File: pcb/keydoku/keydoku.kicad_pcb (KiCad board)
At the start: 2 copper layers, 111 x 99.9 mm, 37 parts

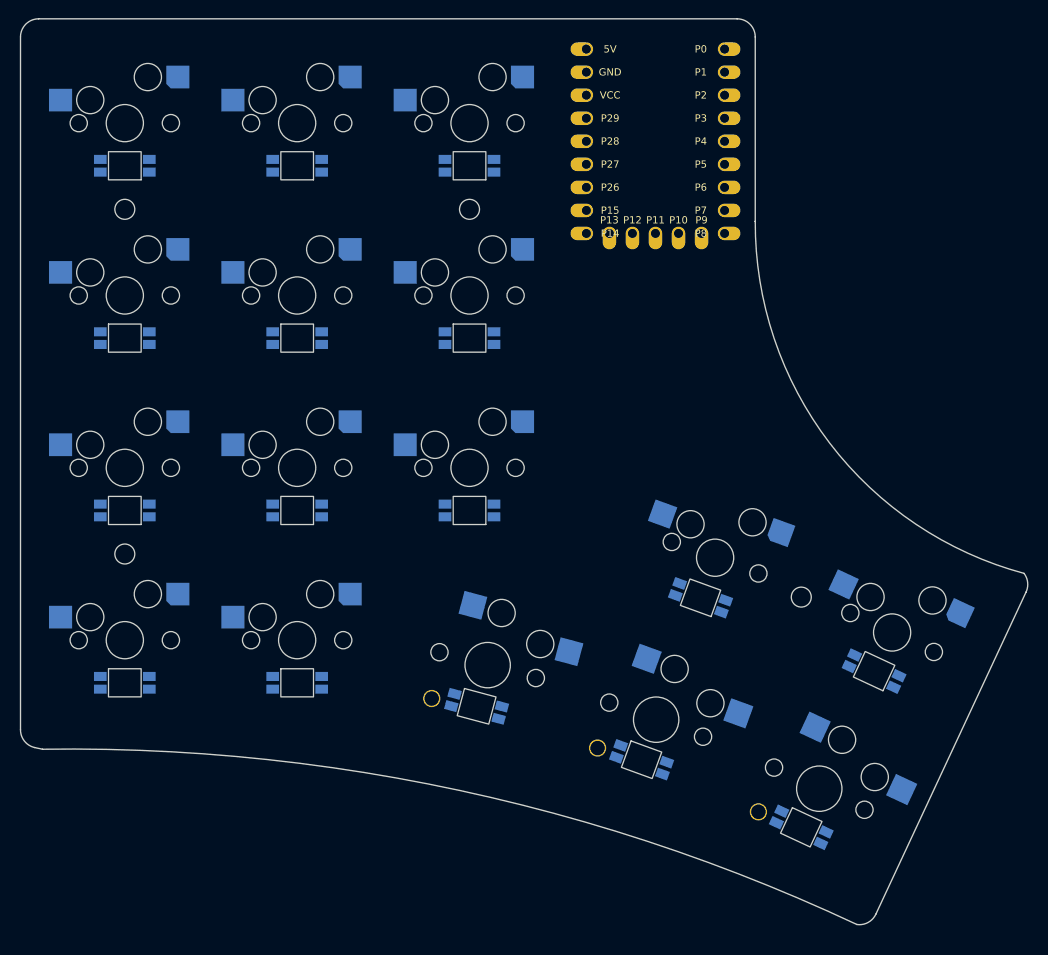
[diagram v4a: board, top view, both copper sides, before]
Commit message: Adding CTC logo as a footprint
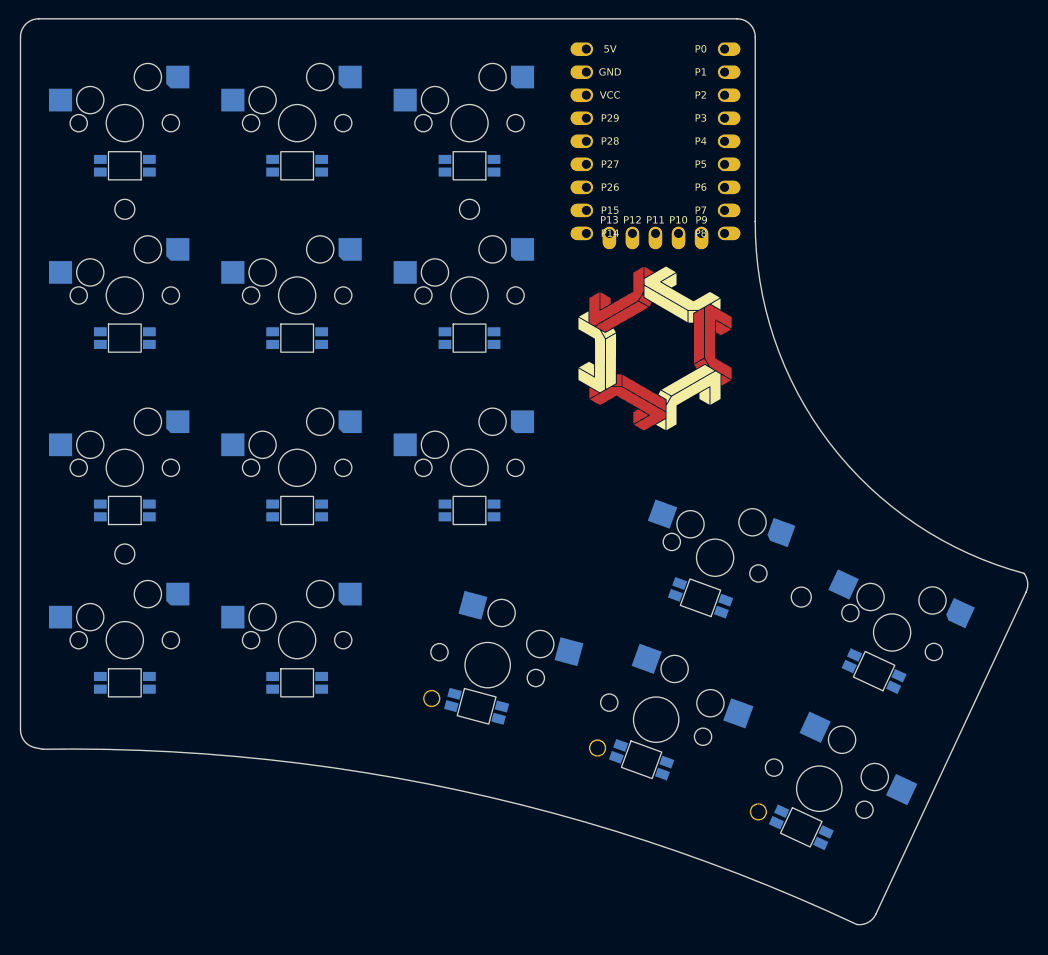
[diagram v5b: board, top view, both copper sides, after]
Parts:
- added G***: LOGO, Project:ctc, F.Cu at (158.4, 117.8)

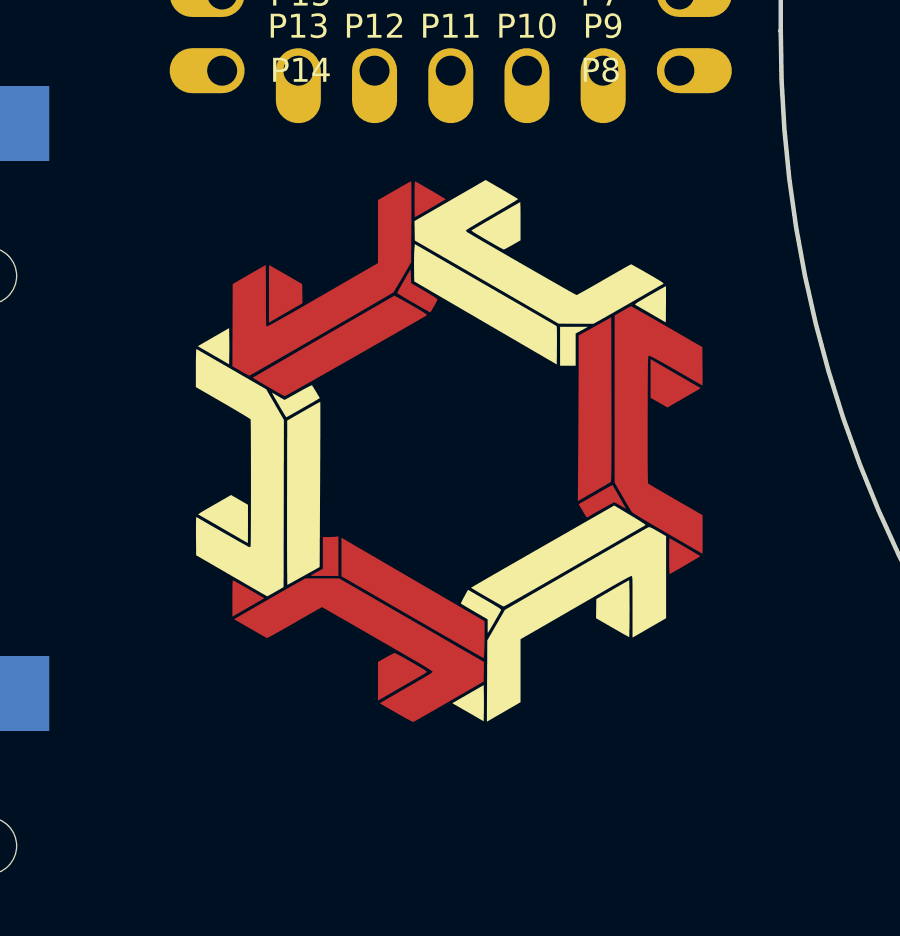
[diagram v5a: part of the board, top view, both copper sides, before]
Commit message: Rotate per key leds and add CTC footprint
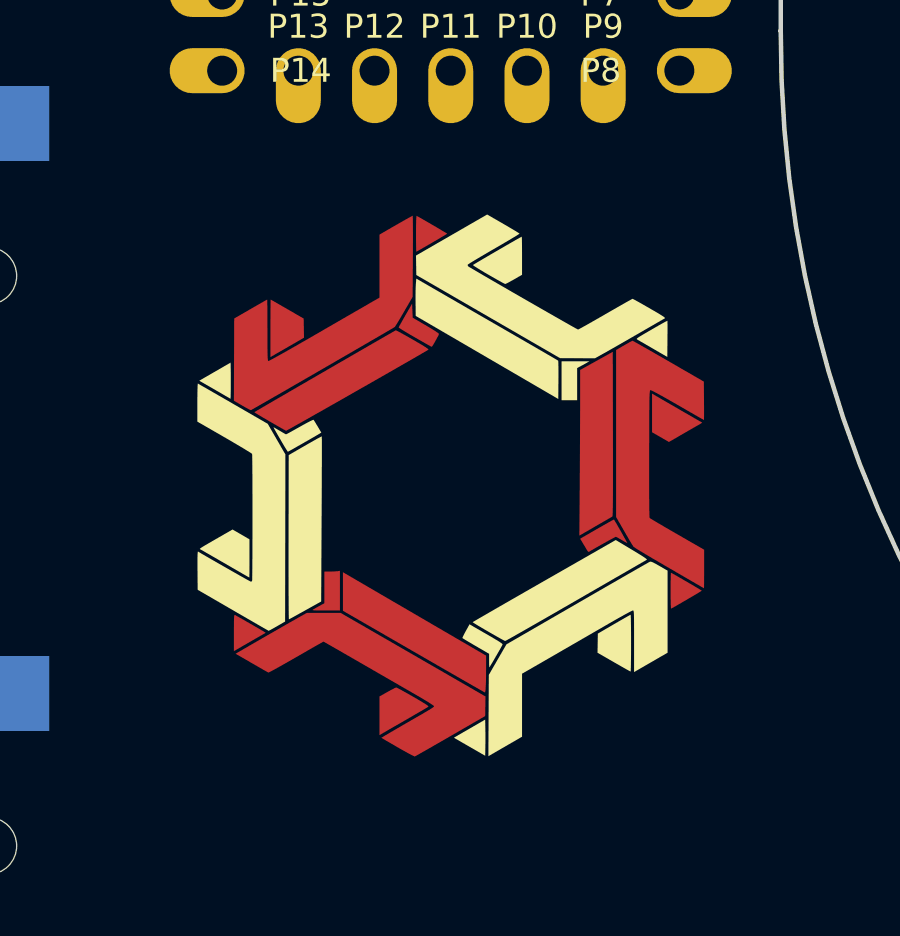
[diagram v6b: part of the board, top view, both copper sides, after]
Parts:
- moved G*** 1.15 mm to (158.5, 119.0)

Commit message: VCC traces in place
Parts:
- moved LED16 1.23 mm to (174.7, 171.9)
- moved LED5 1.23 mm to (138.1, 136.9)
- moved MH1 1.23 mm to (100.1, 103.7)
- moved LED15 1.23 mm to (157.1, 164.4)
- moved MH3 1.23 mm to (100.1, 141.7)
- moved S14 1.23 mm to (140.1, 154.0)
- moved LED6 1.23 mm to (138.1, 98.9)
- moved LED13 1.23 mm to (138.1, 117.9)
- moved LED1 1.23 mm to (100.1, 136.9)
- moved LED4 1.23 mm to (119.1, 98.9)
- moved MH4 1.23 mm to (174.7, 146.5)
- moved LED14 1.23 mm to (138.9, 158.5)
- moved S1 1.23 mm to (100.1, 151.2)
- moved S5 1.23 mm to (119.1, 151.2)
- moved MCU1 1.23 mm to (158.6, 96.2)
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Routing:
- net VCC5V: track 0.00 -> 375.3 mm, vias 0 -> 6

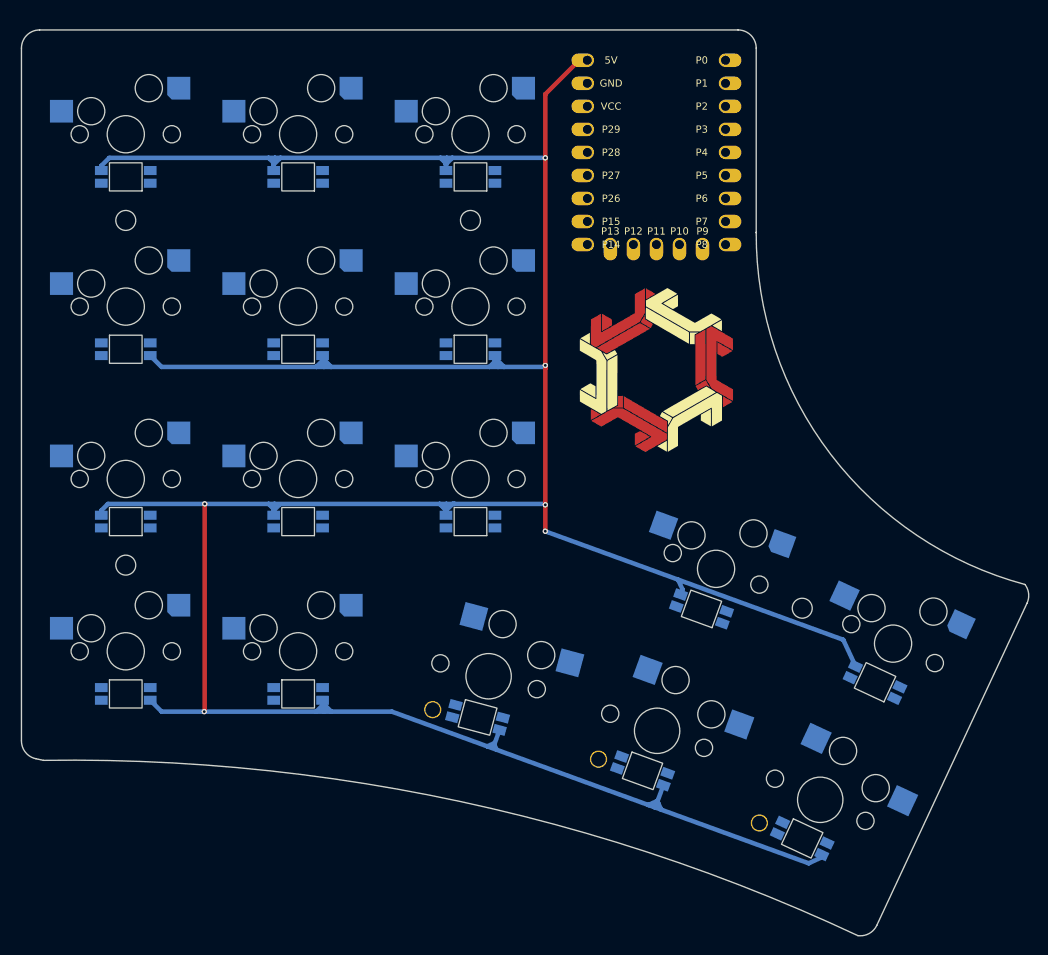
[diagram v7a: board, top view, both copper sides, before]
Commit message: All traces except GND
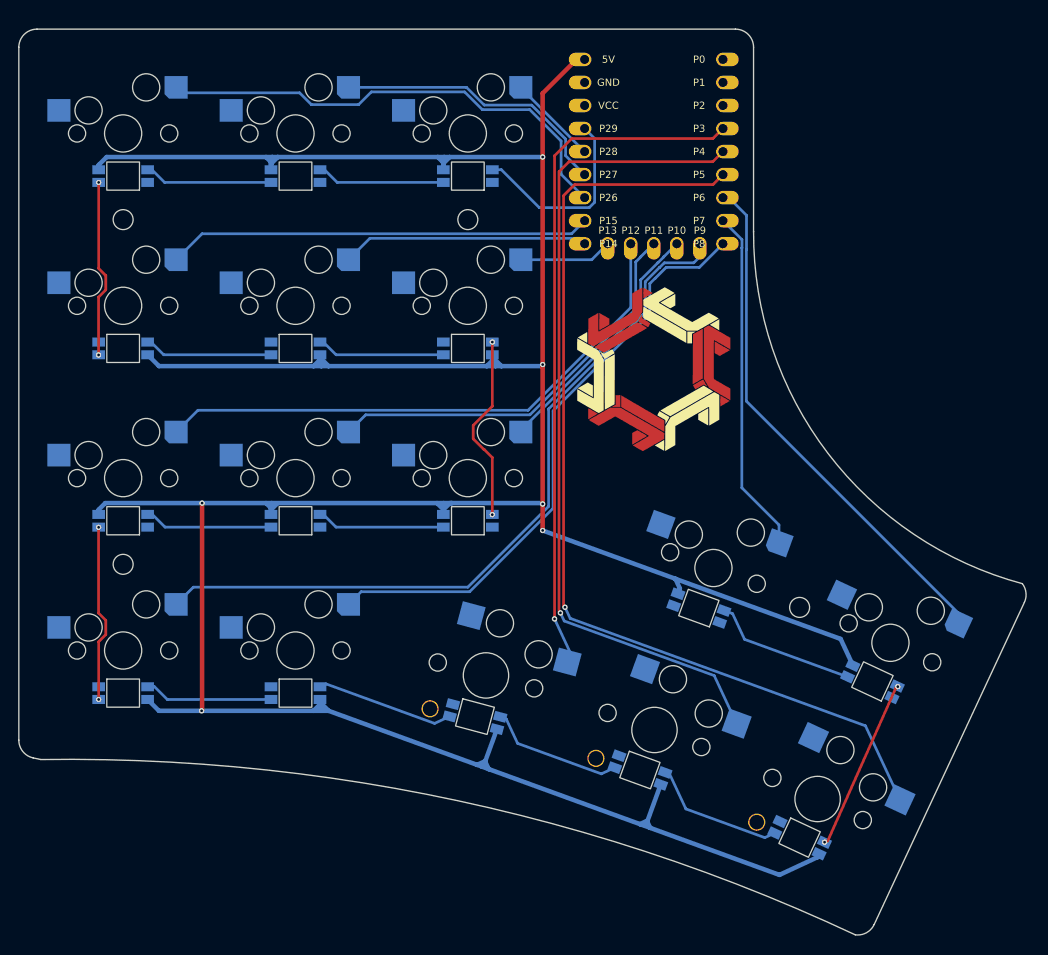
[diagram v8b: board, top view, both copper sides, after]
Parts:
- moved LED12 0.30 mm to (118.8, 117.8)
- moved LED8 0.30 mm to (182.4, 154.5)
- moved S5 0.30 mm to (118.8, 151.1)
- moved LED16 0.30 mm to (174.4, 171.8)
- moved S7 0.30 mm to (118.8, 113.1)
- moved S16 0.30 mm to (176.4, 167.5)
- moved LED7 0.30 mm to (163.3, 146.5)
- moved S12 0.30 mm to (164.9, 142.0)
- moved G*** 0.30 mm to (158.3, 120.1)
- moved MCU1 0.30 mm to (158.3, 96.1)
- moved LED10 0.30 mm to (99.8, 117.8)
- moved LED6 0.30 mm to (137.8, 98.8)
- moved MH1 0.30 mm to (99.8, 103.6)
- moved S2 0.30 mm to (99.8, 132.1)
- moved S9 0.30 mm to (137.8, 132.1)
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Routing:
- net P5: track 0.00 -> 109.0 mm, vias 0 -> 1
- net P4: track 0.00 -> 92.3 mm, vias 0 -> 1
- net P9: track 0.00 -> 83.3 mm
- net P3: track 0.00 -> 76.1 mm, vias 0 -> 1
- net P8: track 0.00 -> 66.0 mm
- net P12: track 0.00 -> 62.8 mm
- net P6: track 0.00 -> 58.1 mm
- net P26: track 0.00 -> 53.4 mm
- net P15: track 0.00 -> 46.8 mm
- net P11: track 0.00 -> 45.3 mm
- net P7: track 0.00 -> 38.1 mm
- net P27: track 0.00 -> 31.1 mm
- net P10: track 0.00 -> 27.9 mm
- net P14: track 0.00 -> 27.3 mm
- net LED_1: track 0.00 -> 21.8 mm
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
